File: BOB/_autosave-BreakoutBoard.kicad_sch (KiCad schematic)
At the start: 2 parts, among them J3 1706013

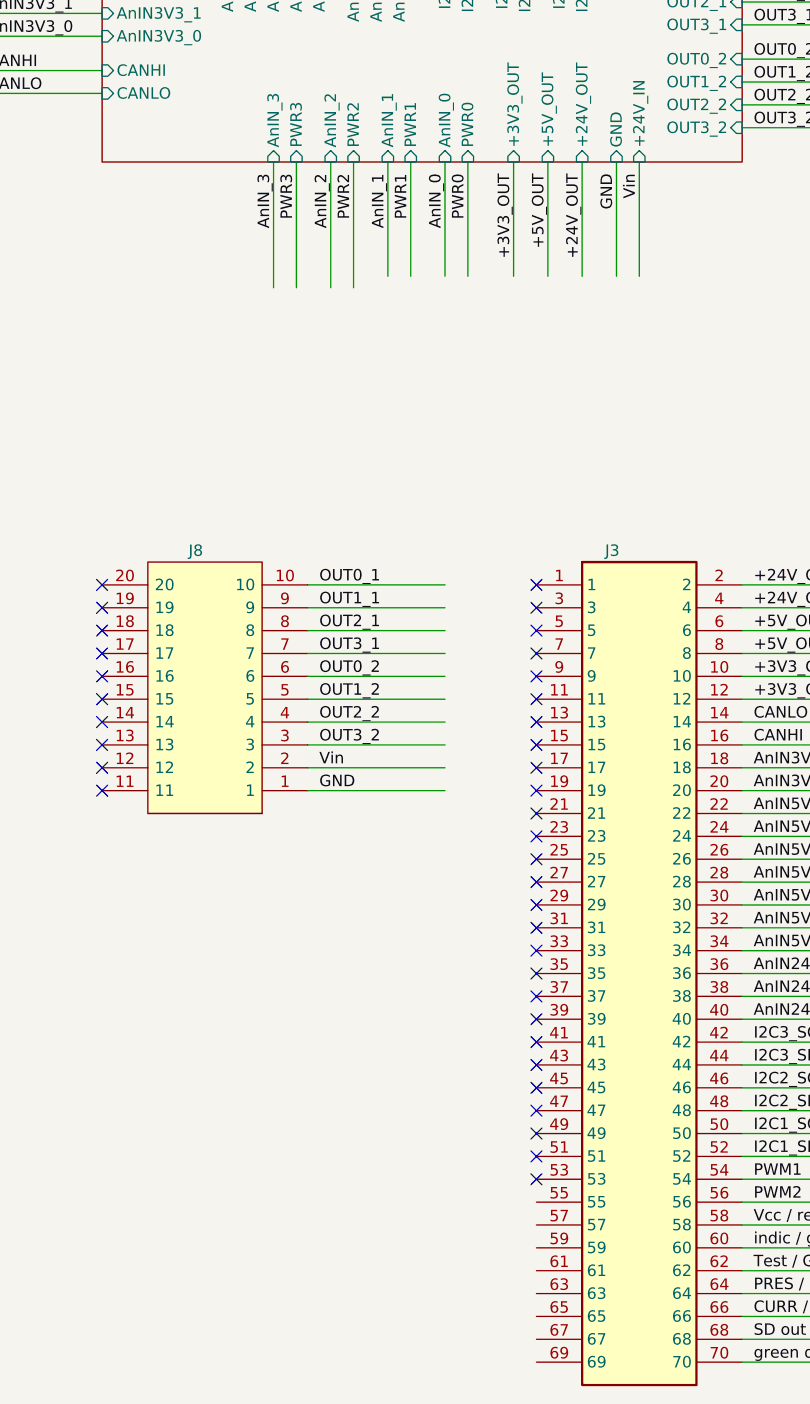
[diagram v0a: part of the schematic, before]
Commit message: BOB v2.2
- New connector for OUT signals and input power pins (Connection for filter modules is not available on this version due to the size of connectors and maximum length of the board)
- Added two big holes for better and more stable connection in the car
- New layout and support for Nodes v2.2
- Created a combined design of 2.54mm connector for more efficient area usage
- PDF schematic added
- Other small visual changes

TODO:
- Change TSAL connection design, because of this issue the labels are not aligned
- Try to use double row connectors instead of just one row for more efficient space usage
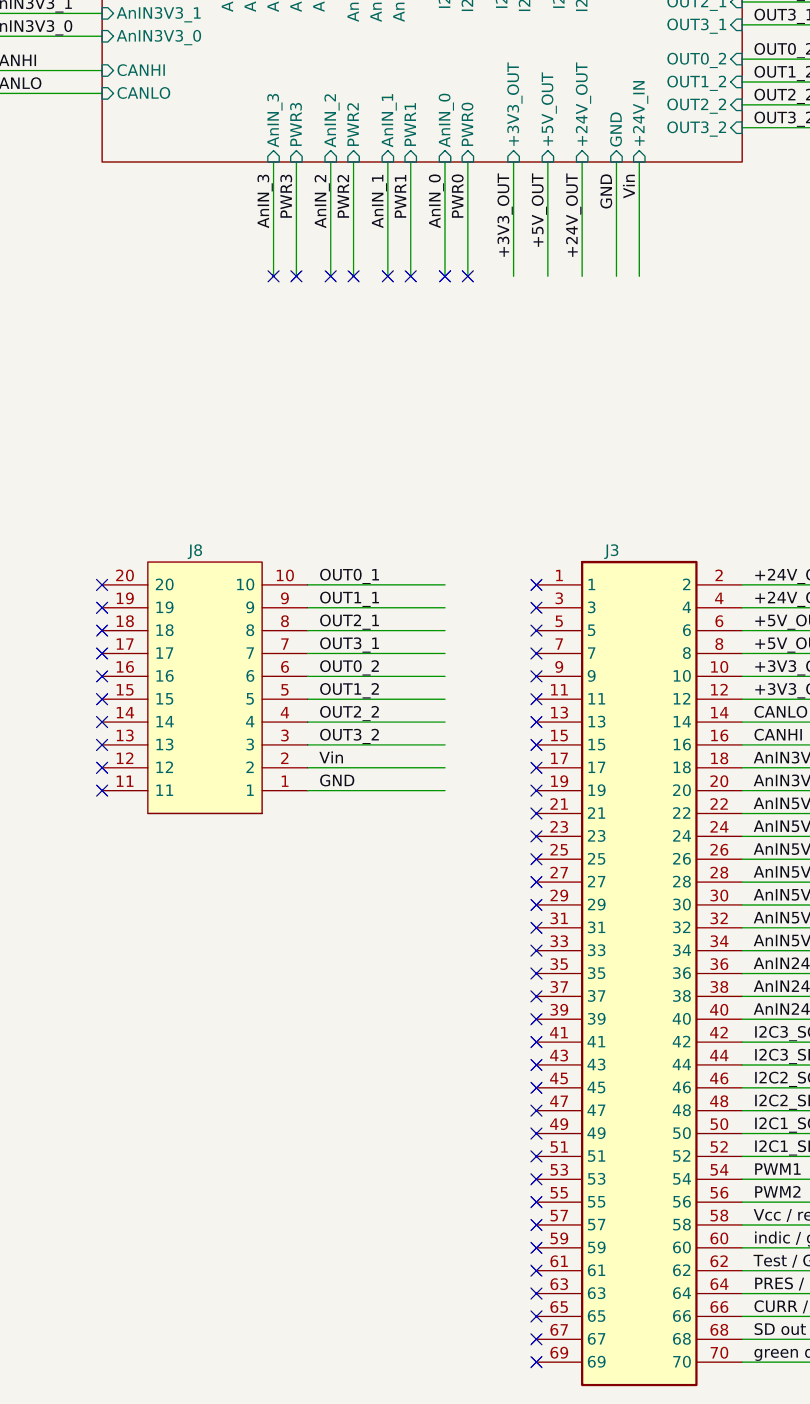
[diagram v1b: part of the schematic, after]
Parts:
- J3: footprint Connector_Phoenix_SPT:1706013 -> Connector_Phoenix_SPT:35_con_Phoenix; symbol 1706013:1706013 -> Connector:35_con_Phoenix; Height 12.6 -> (none); Manufacturer_Name Phoenix Contact -> (none); Manufacturer_Part_Number 1706013 -> (none); Mouser Part Number 651-1706013 -> (none); Mouser Price/Stock https://www.mouser.com/Search/Refine.aspx?Keyword=651-17060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 -> (none)
- J8: symbol Connector:1868115 -> Connector:10_pin_7.62_Phoenix
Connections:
- no-connect marks 37 -> 53
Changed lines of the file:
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@@
+	)
+	(no_connect
+		(at 147.32 246.38)
 	)
 	(no_connect
@@
 	)
 	(no_connect
+		(at 147.32 259.08)
+	)
+	(no_connect
+		(at 127 138.43)
+	)
+	(no_connect
+		(at 120.65 138.43)
+	)
+	(no_connect
 		(at 147.32 238.76)
 	)
 	(no_connect
+		(at 147.32 254)
+	)
+	(no_connect
 		(at 99.06 193.04)
 	)
 	(no_connect
+		(at 147.32 251.46)
+	)
+	(no_connect
+		(at 147.32 243.84)
+	)
+	(no_connect
 		(at 147.32 228.6)
 	)
@@
 	)
 	(no_connect
+		(at 124.46 138.43)
+	)
+	(no_connect
 		(at 147.32 175.26)
 	)
@@
 	)
 	(no_connect
+		(at 137.16 138.43)
+	)
+	(no_connect
 		(at 99.06 172.72)
 	)
@@
 	)
 	(no_connect
+		(at 139.7 138.43)
+	)
+	(no_connect
 		(at 147.32 205.74)
 	)
 	(no_connect
+		(at 147.32 241.3)
+	)
+	(no_connect
 		(at 147.32 233.68)
 	)
@@
 	)
 	(no_connect
+		(at 147.32 248.92)
+	)
+	(no_connect
+		(at 118.11 138.43)
+	)
+	(no_connect
 		(at 147.32 200.66)
 	)
@@
 	)
 	(no_connect
+		(at 133.35 138.43)
+	)
+	(no_connect
 		(at 147.32 213.36)
 	)
@@
 	)
 	(no_connect
+		(at 130.81 138.43)
+	)
+	(no_connect
 		(at 147.32 193.04)
 	)
@@
 	)
 	(no_connect
+		(at 147.32 256.54)
+	)
+	(no_connect
 		(at 147.32 198.12)
 	)
@@
 	(wire
 		(pts
+			(xy 118.11 138.43) (xy 118.11 125.73)
+		)
+		(stroke
+			(width 0)
+			(type default)
+		)
+	)
+	(wire
+		(pts
 			(xy 170.18 114.3) (xy 182.88 114.3)
 		)
@@
 	(wire
 		(pts
-			(xy 118.11 125.73) (xy 118.11 139.7)
-		)
-		(stroke
-			(width 0)
-			(type default)
-		)
-	)
-	(wire
-		(pts
 			(xy 170.18 218.44) (xy 191.77 218.44)
 		)
@@
 	(wire
 		(pts
-			(xy 127 125.73) (xy 127 139.7)
+			(xy 127 125.73) (xy 127 138.43)
 		)
 		(stroke
@@
 	(wire
 		(pts
-			(xy 124.46 125.73) (xy 124.46 139.7)
+			(xy 124.46 125.73) (xy 124.46 138.43)
 		)
 		(stroke
@@
 	(wire
 		(pts
-			(xy 120.65 125.73) (xy 120.65 139.7)
+			(xy 120.65 125.73) (xy 120.65 138.43)
 		)
 		(stroke
@@
 	)
 	(symbol
-		(lib_id "Connector:1868115")
+		(lib_id "Connector:10_pin_7.62_Phoenix")
 		(at 121.92 195.58 180)
 		(unit 1)
@@
 	)
 	(symbol
-		(lib_id "1706013:1706013")
+		(lib_id "Connector:35_con_Phoenix")
 		(at 147.32 172.72 0)
 		(unit 1)
@@
 			)
 		)
-		(property "Footprint" "Connector_Phoenix_SPT:1706013"
+		(property "Footprint" "Connector_Phoenix_SPT:35_con_Phoenix"
 			(at 166.37 267.64 0)
 			(effects
@@
 			)
 		)
-		(property "Description" "PCB terminal block, nominal current: 6 A 160 V number of potentials: 20 pitch: 2.54 mm"
+		(property "Description" ""
 			(at 147.828 163.322 0)
 			(effects
@@
 				(hide yes)
 			)
-		)
-		(property "Height" "12.6"
-			(at 166.37 567.64 0)
-			(effects
-				(font
-					(size 1.27 1.27)
-				)
-				(justify left top)
-				(hide yes)
-			)
-		)
-		(property "Manufacturer_Name" "Phoenix Contact"
-			(at 166.37 667.64 0)
-			(effects
-				(font
-					(size 1.27 1.27)
-				)
-				(justify left top)
-				(hide yes)
-			)
-		)
-		(property "Manufacturer_Part_Number" "1706013"
-			(at 166.37 767.64 0)
-			(effects
-				(font
-					(size 1.27 1.27)
-				)
-				(justify left top)
-				(hide yes)
-			)
-		)
-		(property "Mouser Part Number" "651-1706013"
-			(at 166.37 867.64 0)
-			(effects
-				(font
-					(size 1.27 1.27)
-				)
-				(justify left top)
-				(hide yes)
-			)
-		)
-		(property "Mouser Price/Stock" "https://www.mouser.com/Search/Refine.aspx?Keyword=651-1706013"
-			(at 166.37 967.64 0)
-			(effects
-				(font
-					(size 1.27 1.27)
-				)
-				(justify left top)
-				(hide yes)
-			)
-		)
-		(property "Arrow Part Number" ""
-			(at 166.37 1067.64 0)
-			(effects
-				(font
-					(size 1.27 1.27)
-				)
-				(justify left top)
-				(hide yes)
-			)
-		)
-		(property "Arrow Price/Stock" ""
-			(at 166.37 1167.64 0)
-			(effects
-				(font
-					(size 1.27 1.27)
-				)
-				(justify left top)
-				(hide yes)
-			)
